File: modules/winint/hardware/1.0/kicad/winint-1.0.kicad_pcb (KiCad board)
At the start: 2 copper layers, 75 x 75 mm, 70 parts, among them J1 Screw_Terminal_01x09, J2 Screw_Terminal_01x09, J3 Screw_Terminal_01x03, J4 Screw_Terminal_01x03, J5 Screw_Terminal_01x05, K1 SANYOU_SRD_Form_C, K2 SANYOU_SRD_Form_C, Q1 2N2219, Q2 2N2219, SW1 INSTANCE, U1 ROT, U2 DOK, U3 STP, U4 DEP, U5 RET, U6 OVL, U7 Teensy_3.2, U8 MCP2551-I-P, U9 TEC2-2411WI

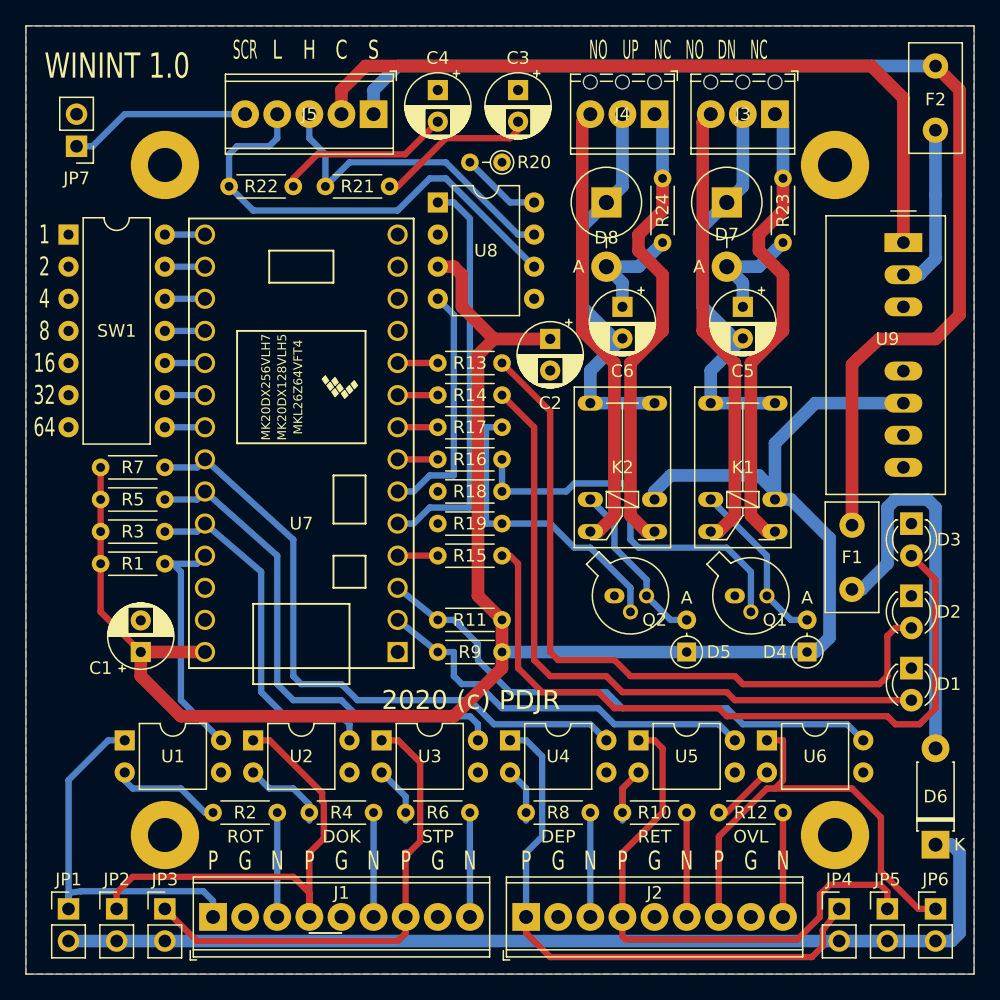
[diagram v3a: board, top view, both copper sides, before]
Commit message: Revised PCB layout
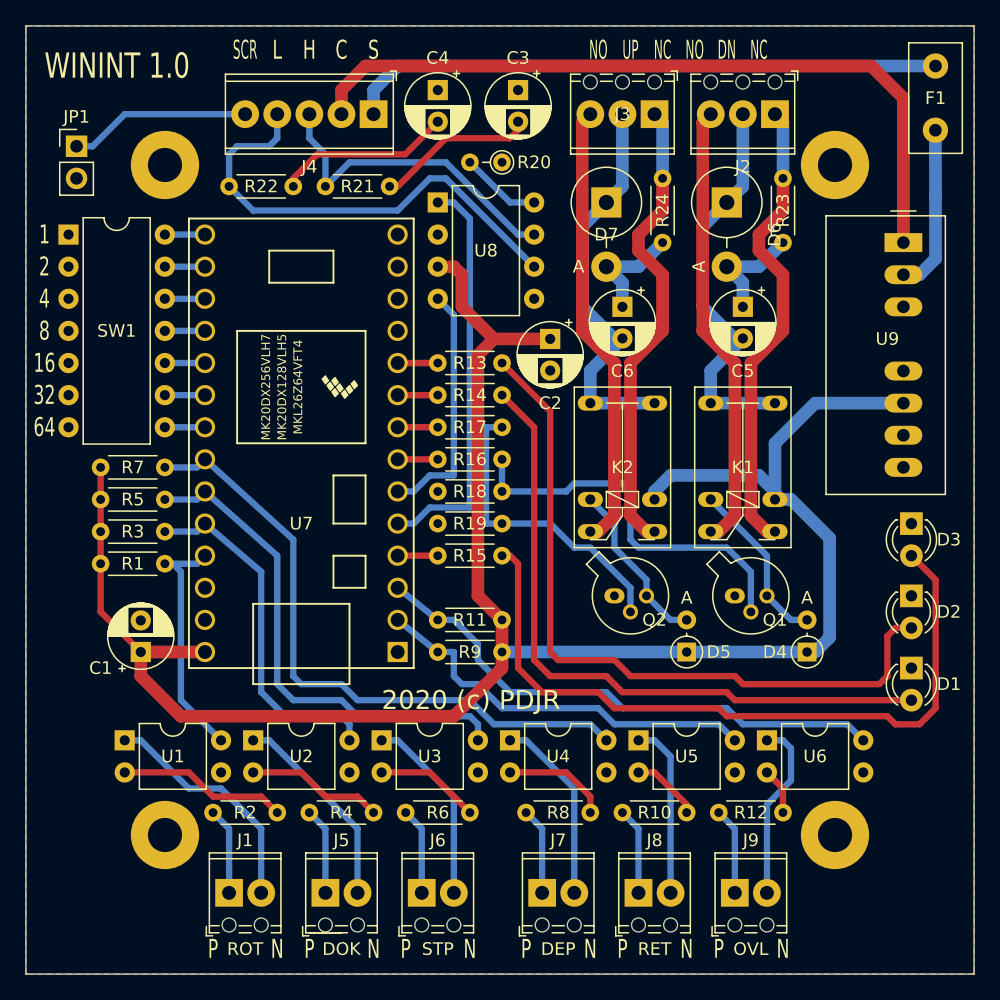
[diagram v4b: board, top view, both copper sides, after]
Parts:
- removed D8: D_TVS, Diode_THT:D_DO-27_P5.08mm_Vertical_AnodeUp
- removed F2: 1A, Fuse:Fuse_Littelfuse_395Series
- removed JP2, JP3, JP4, JP5, JP6, JP7: SCR, Connector_PinHeader_2.54mm:PinHeader_1x02_P2.54mm_Vertical
- added J6: STP, TerminalBlock_Phoenix:TerminalBlock_Phoenix_MPT-0,5-2-2.54_1x02_P2.54mm_Horizontal, F.Cu at (167.3, 155.6)
- added J7: DEP, TerminalBlock_Phoenix:TerminalBlock_Phoenix_MPT-0,5-2-2.54_1x02_P2.54mm_Horizontal, F.Cu at (176.8, 155.6)
- added J8: RET, TerminalBlock_Phoenix:TerminalBlock_Phoenix_MPT-0,5-2-2.54_1x02_P2.54mm_Horizontal, F.Cu at (184.5, 155.6)
- added J9: OVL, TerminalBlock_Phoenix:TerminalBlock_Phoenix_MPT-0,5-2-2.54_1x02_P2.54mm_Horizontal, F.Cu at (192.1, 155.6)
- D1: value DOWN -> UP
- D2: value UP -> DOWN
- D6: value 1N4007 -> D_TVS; footprint Diode_THT:D_DO-41_SOD81_P7.62mm_Horizontal -> Diode_THT:D_DO-27_P5.08mm_Vertical_AnodeUp
- F1: value 100mA -> 1A
- J1: value Screw_Terminal_01x09 -> ROT; footprint TerminalBlock_Phoenix:TerminalBlock_Phoenix_MPT-0,5-9-2.54_1x09_P2.54mm_Horizontal -> TerminalBlock_Phoenix:TerminalBlock_Phoenix_MPT-0,5-2-2.54_1x02_P2.54mm_Horizontal
- J2: value Screw_Terminal_01x09 -> Screw_Terminal_01x03; footprint TerminalBlock_Phoenix:TerminalBlock_Phoenix_MPT-0,5-9-2.54_1x09_P2.54mm_Horizontal -> TerminalBlock_Phoenix:TerminalBlock_Phoenix_MPT-0,5-3-2.54_1x03_P2.54mm_Horizontal
- J4: value Screw_Terminal_01x03 -> Screw_Terminal_01x05; footprint TerminalBlock_Phoenix:TerminalBlock_Phoenix_MPT-0,5-3-2.54_1x03_P2.54mm_Horizontal -> TerminalBlock_Phoenix:TerminalBlock_Phoenix_MPT-0,5-5-2.54_1x05_P2.54mm_Horizontal
- J5: value Screw_Terminal_01x05 -> DOK; footprint TerminalBlock_Phoenix:TerminalBlock_Phoenix_MPT-0,5-5-2.54_1x05_P2.54mm_Horizontal -> TerminalBlock_Phoenix:TerminalBlock_Phoenix_MPT-0,5-2-2.54_1x02_P2.54mm_Horizontal
- K1, K2: value SANYOU_SRD_Form_C -> RS_476-257
- Q1, Q2: value 2N2219 -> NTE123A
- moved J2 66.5 mm to (195.2, 94.0), turned to 180 degrees
- moved J5 61.7 mm to (159.7, 155.6), turned to 0 degrees
- moved JP1 60.3 mm to (140.0, 96.5)
- moved D6 53.4 mm to (191.4, 101.0), turned to 270 degrees
- moved F1 36.9 mm to (207.9, 90.2)
- moved J4 22.2 mm to (163.5, 94.0)
- moved D7 9.53 mm to (181.9, 101.0)
- moved J3 9.53 mm to (185.7, 94.0)
- moved R4 5.08 mm to (163.5, 149.2), turned to 180 degrees
- moved R6 5.08 mm to (171.1, 149.2), turned to 180 degrees
- moved R8 5.08 mm to (180.6, 149.2), turned to 180 degrees
- moved R10 5.08 mm to (188.3, 149.2), turned to 180 degrees
- moved R12 5.08 mm to (195.9, 149.2), turned to 180 degrees
- moved R2 5.08 mm to (155.9, 149.2), turned to 180 degrees
- moved J1 2.29 mm to (152.1, 155.6)
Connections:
- D6 pad 1: /12VDC -> Net-(C5-Pad2)
- D6 pad 2: Net-(D6-Pad2) -> Net-(C5-Pad1)
- D7 pad 1: Net-(C5-Pad2) -> Net-(C6-Pad2)
- D7 pad 2: Net-(C5-Pad1) -> Net-(C6-Pad1)
- F1 pad 2: Net-(D6-Pad2) -> Net-(F1-Pad2)
- J1 pad 2: GND -> Net-(J1-Pad2)
- J2 pad 2: GND -> Net-(C5-Pad2)
- J3 pad 2: Net-(C5-Pad2) -> Net-(C6-Pad2)
- J4 pad 1: Net-(J4-Pad1) -> /NETS
- J4 pad 2: Net-(C6-Pad2) -> /NETC
- J4 pad 3: Net-(J4-Pad3) -> /CANH
- J5 pad 1: /NETS -> Net-(J5-Pad1)
- J5 pad 2: /NETC -> Net-(J5-Pad2)
- JP1 pad 1: Net-(J1-Pad1) -> /SHIELD
- JP1 pad 2: /12VDC -> GND
- K1 pad 1: Net-(J3-Pad1) -> Net-(J2-Pad1)
- K1 pad 10: Net-(J3-Pad3) -> Net-(J2-Pad3)
- K2 pad 1: Net-(J4-Pad1) -> Net-(J3-Pad1)
- K2 pad 10: Net-(J4-Pad3) -> Net-(J3-Pad3)
- R10 pad 2: Net-(J2-Pad6) -> Net-(J8-Pad1)
- R12 pad 2: Net-(J2-Pad9) -> Net-(J9-Pad1)
- R2 pad 2: Net-(J1-Pad3) -> Net-(J1-Pad1)
- R23 pad 2: Net-(J3-Pad1) -> Net-(J2-Pad1)
- R24 pad 2: Net-(J4-Pad1) -> Net-(J3-Pad1)
- R4 pad 2: Net-(J1-Pad6) -> Net-(J5-Pad1)
- R6 pad 2: Net-(J1-Pad9) -> Net-(J6-Pad1)
- R8 pad 2: Net-(J2-Pad3) -> Net-(J7-Pad1)
- U1 pad 1: Net-(J1-Pad1) -> Net-(J1-Pad2)
- U2 pad 1: Net-(J1-Pad4) -> Net-(J5-Pad2)
- U3 pad 1: Net-(J1-Pad7) -> Net-(J6-Pad2)
- U4 pad 1: Net-(J2-Pad1) -> Net-(J7-Pad2)
- U5 pad 1: Net-(J2-Pad4) -> Net-(J8-Pad2)
- U6 pad 1: Net-(J2-Pad7) -> Net-(J9-Pad2)
- U9 pad 2: Net-(F2-Pad2) -> Net-(F1-Pad2)
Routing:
- net /12VDC: track 79.3 -> 0.00 mm
- net Net-(J2-Pad4): track 43.8 -> 0.00 mm
- net /NETS: track 90.4 -> 47.1 mm
- net Net-(J1-Pad7): track 38.3 -> 0.00 mm
- net Net-(J4-Pad1): track 37.1 -> 0.00 mm
- net Net-(J1-Pad4): track 37.0 -> 0.00 mm
- net Net-(J2-Pad7): track 36.9 -> 0.00 mm
- net Net-(J4-Pad3): track 35.5 -> 0.00 mm
- net Net-(D6-Pad2): track 31.5 -> 0.00 mm
- net Net-(J2-Pad3): track 7.62 -> 35.5 mm
- net Net-(J1-Pad1): track 30.2 -> 6.88 mm
- net Net-(J1-Pad2): track 0.00 -> 18.8 mm
- net Net-(J5-Pad2): track 0.00 -> 16.2 mm
- net Net-(J6-Pad2): track 0.00 -> 15.2 mm
- net Net-(J7-Pad2): track 0.00 -> 14.9 mm
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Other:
- board text removed: "G"
